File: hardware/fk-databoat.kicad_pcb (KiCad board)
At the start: 2 copper layers, 96.5 x 81.3 mm, 19 parts, among them J1 CONN_01X02, J2 CONN_01X02, P1 CONN_01X03, P2 CONN_01X03, P3 CONN_01X03, P4 CONN_01X03, P5 CONN_01X03, U1 VISO, U10 SERIAL_PORT_EXPANDER, U11 ATLAS_SENSOR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

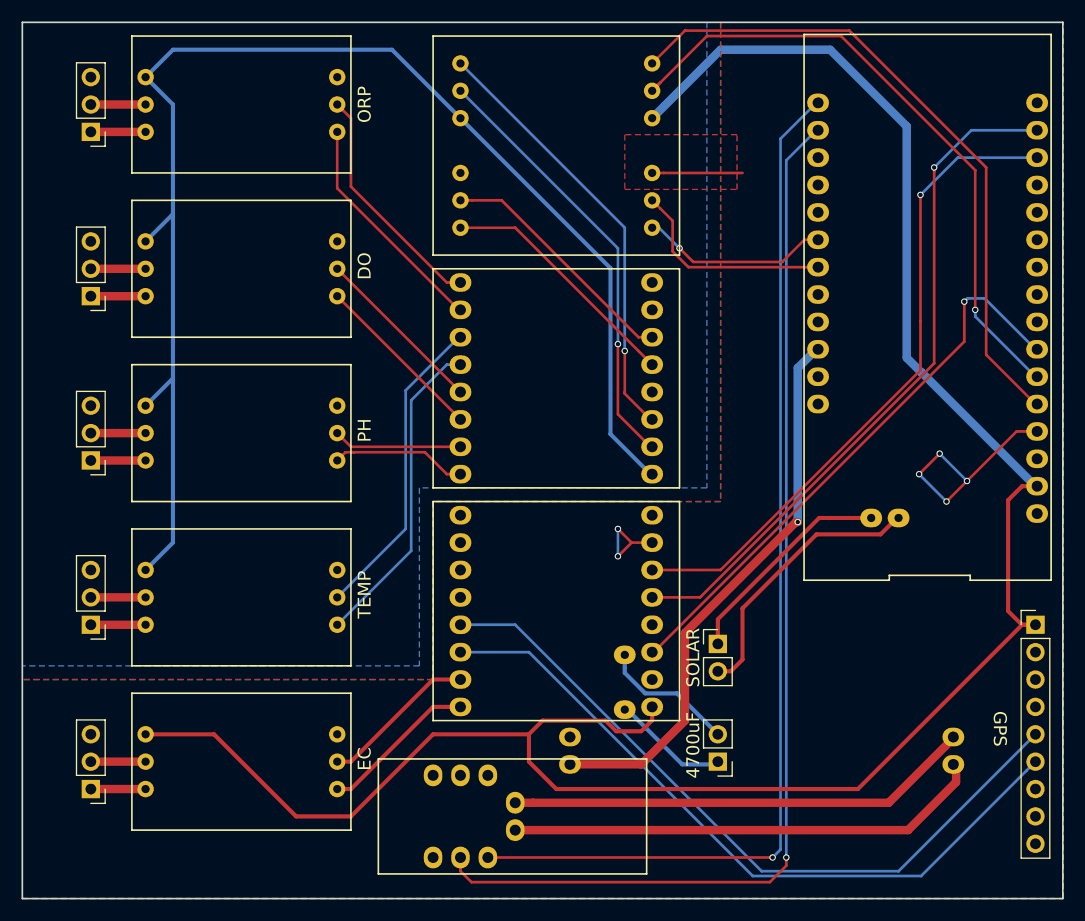
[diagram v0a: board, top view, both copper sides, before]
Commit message: Fix E and S1 GND issues on SPE. Add logo/version.
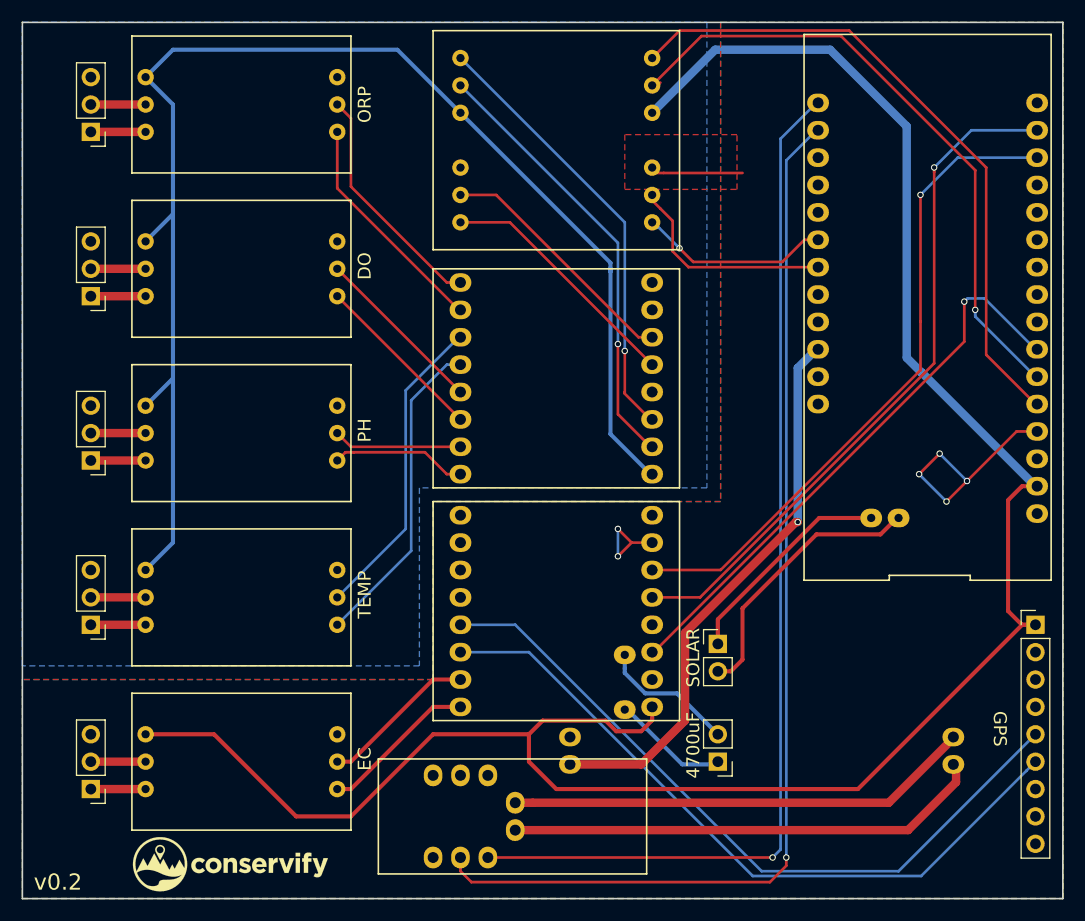
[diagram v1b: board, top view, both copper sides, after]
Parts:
- added G***: LOGO, conservify:conservify_text_negative_4000, F.Cu at (176.8, 149.2)
- U10, U3: value SERIAL_PORT_EXPANDER -> SERIAL_PORT_EXPANDER_4
- moved U10 21.6 mm to (208.3, 105.4)
- moved U3 21.6 mm to (208.3, 127.0)
- moved U1 0.50 mm to (208.3, 82.0)
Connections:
- U10 pad 1: +3V3 -> /ISO_V
- U10 pad 10: /GPS_TX -> /SPE_ISO_RX1
- U10 pad 11: /GPS_RX -> /SPE_ISO_TX1
- U10 pad 12: Net-(U10-Pad12) -> /SPE_ISO_RX2
- U10 pad 13: Net-(U10-Pad13) -> /SPE_ISO_TX2
- U10 pad 14: Net-(U10-Pad14) -> /SPE_ISO_RX3
- U10 pad 15: Net-(U10-Pad15) -> /SPE_ISO_TX3
- U10 pad 2: GND -> /ISO_GND
- U10 pad 3: /SPE_NOR_SEL_0 -> /INT_SEL_0
- U10 pad 4: Net-(U10-Pad4) -> /INT_SEL_1
- U10 pad 6: /SPE_NOR_TX -> /INT_TX
- U10 pad 7: /SPE_NOR_RX -> /INT_RX
- U10 pad 8: /EC_TX -> /SPE_ISO_RX0
- U10 pad 9: /EC_RX -> /SPE_ISO_TX0
- U3 pad 1: /ISO_V -> +3V3
- U3 pad 10: /SPE_ISO_RX1 -> /GPS_TX
- U3 pad 11: /SPE_ISO_TX1 -> /GPS_RX
- U3 pad 12: /SPE_ISO_RX2 -> Net-(U3-Pad12)
- U3 pad 13: /SPE_ISO_TX2 -> Net-(U3-Pad13)
- U3 pad 14: /SPE_ISO_RX3 -> Net-(U3-Pad14)
- U3 pad 15: /SPE_ISO_TX3 -> Net-(U3-Pad15)
- U3 pad 2: /ISO_GND -> GND
- U3 pad 3: /INT_SEL_0 -> /SPE_NOR_SEL_0
- U3 pad 4: /INT_SEL_1 -> GND
- U3 pad 6: /INT_TX -> /SPE_NOR_TX
- U3 pad 7: /INT_RX -> /SPE_NOR_RX
- U3 pad 8: /SPE_ISO_RX0 -> /EC_TX
- U3 pad 9: /SPE_ISO_TX0 -> /EC_RX
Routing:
- net /ISO_V: track 128.4 -> 129.0 mm
- net /INT_SEL_1: track 40.5 -> 41.0 mm
- net /INT_SEL_0: track 40.5 -> 41.0 mm
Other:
- board text added: "v0.2"

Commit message: Fixing GPS orientation.
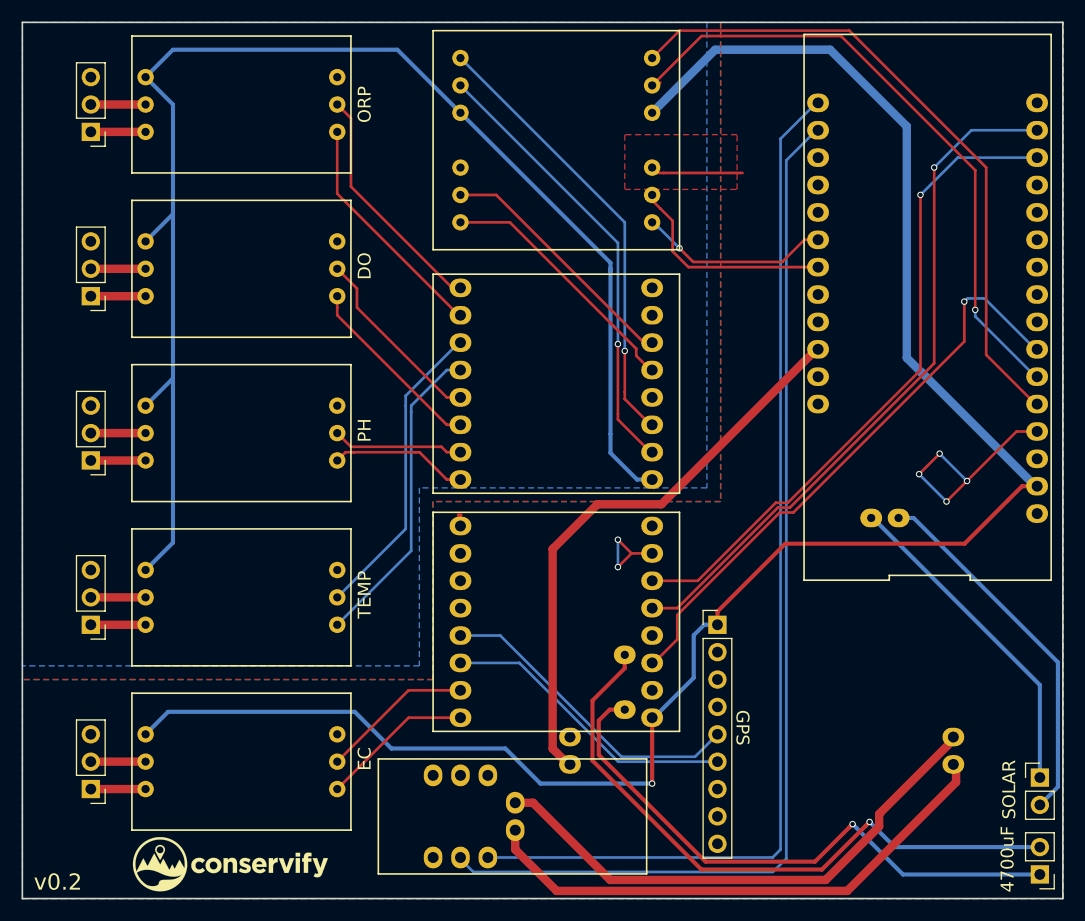
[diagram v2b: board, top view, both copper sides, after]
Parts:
- moved J2 32.3 mm to (251.9, 141.2)
- moved J1 31.7 mm to (251.9, 150.2)
- moved U12 29.5 mm to (222.0, 127.0)
- moved U3 1.00 mm to (208.3, 128.0)
- moved U10 0.50 mm to (208.3, 105.9)
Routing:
- net Net-(J1-Pad2): track 12.7 -> 59.5 mm, vias 0 -> 1
- net Net-(J1-Pad1): track 10.5 -> 54.4 mm, vias 0 -> 1
- net /GPS_TX: track 68.1 -> 29.4 mm
- net /GPS_RX: track 66.3 -> 27.6 mm
- net +3V3: track 197.0 -> 172.0 mm, vias 0 -> 1
- net Net-(J2-Pad1): track 20.4 -> 30.6 mm
- net Net-(J2-Pad2): track 25.4 -> 34.4 mm
- net /B-: track 43.4 -> 50.0 mm
- net /B+: track 44.4 -> 50.1 mm
- net /SCL: track 102.1 -> 100.3 mm, vias 1 -> 0
- net /SPE_NOR_SEL_0: track 53.4 -> 55.2 mm
- net /ISO_V: track 129.0 -> 130.4 mm
- net /SPE_ISO_TX1: track 16.2 -> 17.4 mm
- net /SPE_ISO_RX1: track 16.2 -> 17.4 mm
- net /VLOAD: track 52.0 -> 53.2 mm, vias 1 -> 0
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
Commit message: Integrate serial port expander into data boat PCB.
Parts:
- added D1: LED, Resistors_SMD:R_0603_HandSoldering, F.Cu at (227.1, 73.4)
- added D2: LED, Resistors_SMD:R_0603_HandSoldering, F.Cu at (219.6, 73.5)
- added D3: LED, Resistors_SMD:R_0603_HandSoldering, F.Cu at (223.4, 73.5)
- added J3: CONN_01X02, Connectors_JST:JST_PH_S2B-PH-SM4-TB_02x2.00mm_Angled, B.Cu at (179.2, 144.9)
- added Q1: 2N7002, TO_SOT_Packages_SMD:SOT-23, F.Cu at (249.2, 74.6)
- added Q2: 2N7002, TO_SOT_Packages_SMD:SOT-23, F.Cu at (245.2, 74.6)
- added Q3: 2N7002, TO_SOT_Packages_SMD:SOT-23, F.Cu at (241.0, 74.6)
- added R1: R, Resistors_SMD:R_0603_HandSoldering, F.Cu at (228.8, 73.4)
- added R2: R, Resistors_SMD:R_0603_HandSoldering, F.Cu at (221.3, 73.4)
- added R3: R, Resistors_SMD:R_0603_HandSoldering, F.Cu at (225.0, 73.5)
- U10, U3: value SERIAL_PORT_EXPANDER_4 -> 74hc4052; footprint conservify:serial_port_expander_small -> Housings_SOIC:SOIC-16_3.9x9.9mm_Pitch1.27mm
- moved U10 38.4 mm to (237.8, 130.5), turned to 90 degrees
- moved U3 28.3 mm to (199.4, 101.1), turned to 0 degrees
- moved U2 0.20 mm to (241.3, 97.6)
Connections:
- U10 pad 1: /ISO_V -> /EC_RX
- U10 pad 10: /SPE_ISO_RX1 -> /SPE_NOR_SEL_0
- U10 pad 11: /SPE_ISO_TX1 -> Net-(U10-Pad11)
- U10 pad 12: /SPE_ISO_RX2 -> /EC_TX
- U10 pad 13: /SPE_ISO_TX2 -> /SPE_NOR_RX
- U10 pad 14: /SPE_ISO_RX3 -> /GPS_TX
- U10 pad 15: /SPE_ISO_TX3 -> Net-(U10-Pad15)
- U10 pad 2: /ISO_GND -> Net-(U10-Pad2)
- U10 pad 3: /INT_SEL_0 -> /SPE_NOR_TX
- U10 pad 4: /INT_SEL_1 -> Net-(U10-Pad4)
- U10 pad 5: /ISO_GND -> /GPS_RX
- U10 pad 6: /INT_TX -> GND
- U10 pad 7: /INT_RX -> GND
- U10 pad 8: /SPE_ISO_RX0 -> GND
- U10 pad 9: /SPE_ISO_TX0 -> GND
- U2 pad 10: Net-(U2-Pad10) -> /L2
- U2 pad 19: Net-(U2-Pad19) -> /L3
- U2 pad 9: Net-(U2-Pad9) -> /L1
- U3 pad 1: +3V3 -> /SPE_ISO_TX0
- U3 pad 10: /GPS_TX -> /INT_SEL_0
- U3 pad 11: /GPS_RX -> /SPE_ISO_RX3
- U3 pad 12: Net-(U3-Pad12) -> /SPE_ISO_RX0
- U3 pad 13: Net-(U3-Pad13) -> /INT_RX
- U3 pad 14: Net-(U3-Pad14) -> /SPE_ISO_RX1
- U3 pad 15: Net-(U3-Pad15) -> /SPE_ISO_RX2
- U3 pad 2: GND -> /SPE_ISO_TX2
- U3 pad 3: /SPE_NOR_SEL_0 -> /INT_TX
- U3 pad 4: GND -> /SPE_ISO_TX3
- U3 pad 5: GND -> /SPE_ISO_TX1
- U3 pad 6: /SPE_NOR_TX -> /ISO_GND
- U3 pad 7: /SPE_NOR_RX -> /ISO_GND
- U3 pad 8: /EC_TX -> /ISO_GND
- U3 pad 9: /EC_RX -> /INT_SEL_1
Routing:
- net /EC_TX: track 14.2 -> 59.9 mm, vias 0 -> 2
- net /EC_RX: track 14.2 -> 57.8 mm, vias 0 -> 2
- net +3V3: track 172.0 -> 201.8 mm, vias 1 -> 0
- net Net-(Q2-Pad3): track 0.00 -> 26.3 mm
- net /ISO_V: track 130.4 -> 106.5 mm, vias 0 -> 1
- net /L1: track 0.00 -> 23.0 mm
- net GND: track 37.4 -> 59.4 mm, vias 6 -> 10
- net /L2: track 0.00 -> 22.0 mm, vias 0 -> 1
- net Net-(Q1-Pad3): track 0.00 -> 21.9 mm
- net /B+: track 50.1 -> 71.5 mm
- net /B-: track 50.0 -> 71.3 mm
- net /SPE_NOR_SEL_0: track 55.2 -> 37.4 mm, vias 1 -> 0
- net Net-(Q3-Pad3): track 0.00 -> 17.6 mm
- net /SPE_ISO_RX3: track 22.2 -> 38.8 mm, vias 0 -> 1
- net /SPE_ISO_RX0: track 12.2 -> 26.0 mm, vias 0 -> 1
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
